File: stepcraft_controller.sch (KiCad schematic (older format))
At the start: 70 parts, among them J1 USB, J10 4th Axle, J11 Input2 Select, J2 Probe, J3 Spindle, J4 OutSelect, J6 Relay select, J7 Serial, J8 ISP, J9 X1, SW1 RST, U1 CP2102N-A01-GQFN24, U2 ADuM1201BR, U3 ADuM1201BR, U4 ATMEGA328P-AU, Y1 Crystal

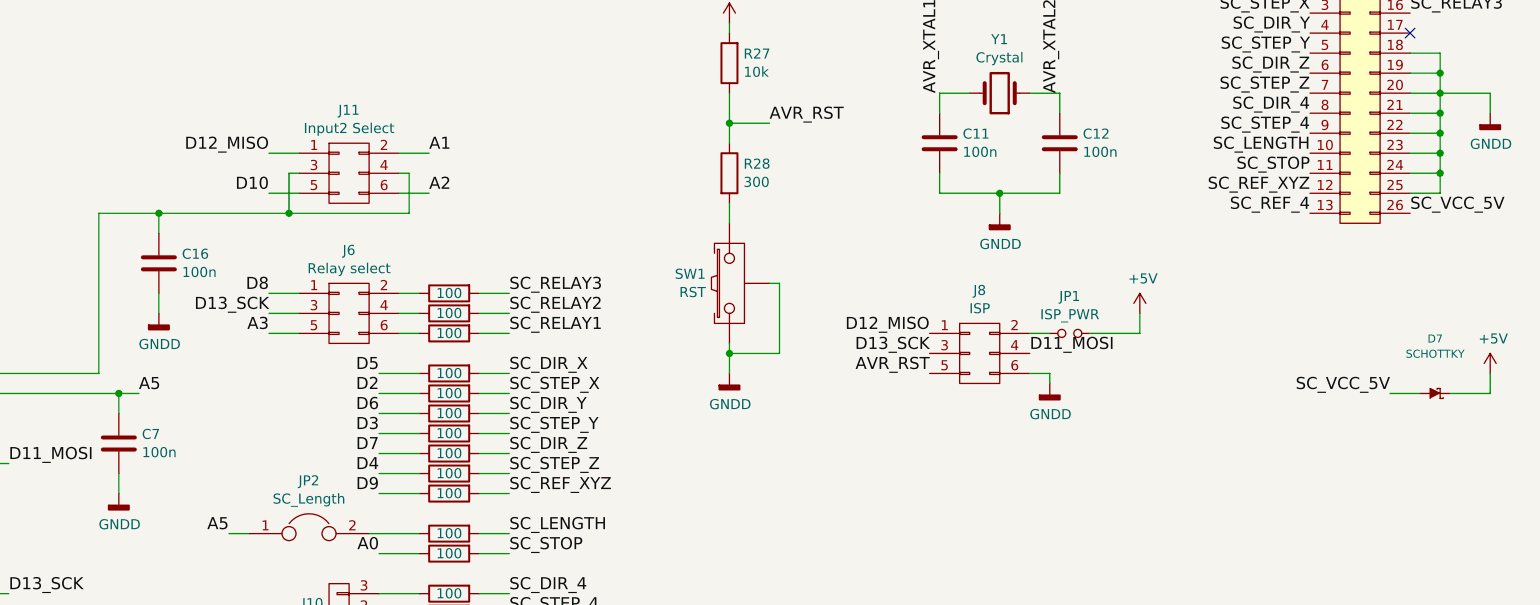
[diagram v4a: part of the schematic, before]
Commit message: Fix Diode symbol (was reversed), input dcouple caps value, X1 caps value, minor routing improvement.
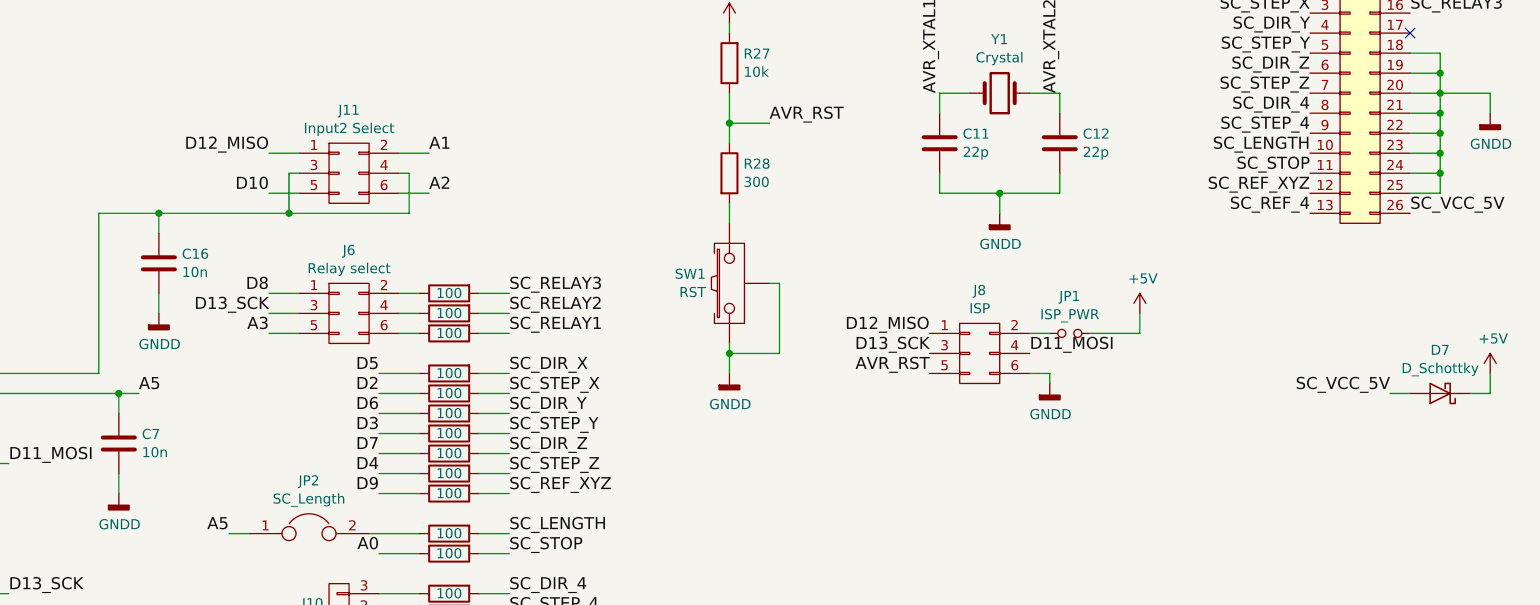
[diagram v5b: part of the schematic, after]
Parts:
- removed D7: SCHOTTKY, Diodes_SMD:D_SOD-123, symbol SCHOTTKY
- added D7: D_Schottky, Diodes_SMD:D_SOD-123, symbol D_Schottky
- C11, C12: value 100n -> 22p
- C16, C7: value 100n -> 10n
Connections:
- net +5V: now also D7.1 (K)
- net SC_VCC_5V: now also D7.2 (A)
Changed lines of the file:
@@
-	1    0    0    -1
-$EndComp
-$Comp
-L SCHOTTKY D7
-U 1 1 59977912
-P 10550 6250
-F 0 "D7" H 10575 6523 40  0000 C CNN
-F 1 "SCHOTTKY" H 10575 6447 40  0000 C CNN
-F 2 "Diodes_SMD:D_SOD-123" H 10575 6356 60  0001 C CNN
-F 3 "" H 10550 6250 60  0000 C CNN
-	1    10550 6250
 	1    0    0    -1
 $EndComp
@@
 P 8100 5000
 F 0 "C11" H 8215 5046 50  0000 L CNN
-F 1 "100n" H 8215 4955 50  0000 L CNN
+F 1 "22p" H 8215 4955 50  0000 L CNN
 F 2 "Capacitors_SMD:C_0805" H 8138 4850 50  0001 C CNN
 F 3 "" H 8100 5000 50  0001 C CNN
@@
 P 8700 5000
 F 0 "C12" H 8815 5046 50  0000 L CNN
-F 1 "100n" H 8815 4955 50  0000 L CNN
+F 1 "22p" H 8815 4955 50  0000 L CNN
 F 2 "Capacitors_SMD:C_0805" H 8738 4850 50  0001 C CNN
 F 3 "" H 8700 5000 50  0001 C CNN
@@
 P 4000 6500
 F 0 "C7" H 4115 6546 50  0000 L CNN
-F 1 "100n" H 4115 6455 50  0000 L CNN
+F 1 "10n" H 4115 6455 50  0000 L CNN
 F 2 "Capacitors_SMD:C_0805" H 4038 6350 50  0001 C CNN
 F 3 "" H 4000 6500 50  0001 C CNN
@@
 P 4200 5600
 F 0 "C16" H 4315 5646 50  0000 L CNN
-F 1 "100n" H 4315 5555 50  0000 L CNN
+F 1 "10n" H 4315 5555 50  0000 L CNN
 F 2 "Capacitors_SMD:C_0805" H 4238 5450 50  0001 C CNN
 F 3 "" H 4200 5600 50  0001 C CNN
@@
 Wire Wire Line
 	7050 4450 7050 4400
-Wire Wire Line
-	10350 6250 10500 6250
-Wire Wire Line
-	10650 6250 10850 6250
 Wire Wire Line
 	5850 2750 5850 2650
@@
 NoConn ~ 3650 2550
 NoConn ~ 3650 2450
+$Comp
+L D_Schottky D7
+U 1 1 59FC710B
+P 10600 6250
+F 0 "D7" H 10600 6034 50  0000 C CNN
+F 1 "D_Schottky" H 10600 6125 50  0000 C CNN
+F 2 "Diodes_SMD:D_SOD-123" H 10600 6250 50  0001 C CNN
+F 3 "" H 10600 6250 50  0001 C CNN
+	1    10600 6250
+	-1   0    0    1
+$EndComp
+Wire Wire Line
+	10350 6250 10450 6250
+Wire Wire Line
+	10750 6250 10850 6250
 $EndSCHEMATC

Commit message: Update to Kicad 5, add remarks about galvanic isolation
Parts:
- added R29: 10k (DNP), Resistors_SMD:R_0805, symbol Device:R
- C1, C10, C11, C12, C13, C14, C15, C16, C2, C3, C4, C5, C6, C7, C8, C9: symbol C -> Device:C
- D1, D2, D3, D4, D5, D6: value D_TVS -> TVS Diode; footprint Capacitors_SMD:C_0603 -> Diode_SMD:D_0603_1608Metric; symbol D_TVS -> Device:D_TVS
- D7: symbol D_Schottky -> Device:D_Schottky
- F1: symbol Polyfuse -> Device:Polyfuse
- J1: footprint iotta_footprints:conn_usb_B_micro_smd -> iotta_footprints:USB_Micro-B_2_Holes; symbol USB_OTG -> stepcraft_controller-rescue:USB_OTG
- J10, J4: symbol CONN_01X03 -> stepcraft_controller-rescue:CONN_01X03
- J11, J6, J8: symbol CONN_02X03 -> stepcraft_controller-rescue:CONN_02X03
- J2, J3: symbol Audio-Jack-3 -> stepcraft_controller-rescue:Audio-Jack-3
- J7: symbol CONN_01X02 -> stepcraft_controller-rescue:CONN_01X02
- J9: symbol Stepcraft_X1 -> iotta_wsn_rev2:Stepcraft_X1
- JP1: symbol Jumper_NO_Small -> Device:Jumper_NO_Small
- JP2: symbol Jumper -> Device:Jumper
- R1, R10, R11, R12, R13, R14, R15, R16, R17, R18, R19, R2, R20, R21, R22, R23, R24, R25, R26, R27, R28, R3, R4, R5, R6, R7, R8, R9: symbol R -> Device:R
- SW1: symbol SW_PUSH_SHIELD -> iotta_wsn_rev2:SW_PUSH_SHIELD
- U1: symbol CP2102N-A01-GQFN24 -> stepcraft_controller-rescue:CP2102N-A01-GQFN24
- U2, U3: symbol ADuM1201BR -> stepcraft_controller-rescue:ADuM1201BR
- U4: symbol ATMEGA328P-AU -> stepcraft_controller-rescue:ATMEGA328P-AU
- Y1: symbol Crystal -> Device:Crystal
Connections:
- net +5V: now also R29.2
- net AVR_RST: now also R29.1
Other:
- note added: "For use without galvanic separation:\n\n- Do not place U2 and U3 \n- Do not place C5, C6, C8, C9, R9, R10, R11\n- Place R5, R6, R7, R8"
- note added: "TVS Diodes, use for example Wurth 82356050050 \nProbably any 5V TVS/ESD suppressor will work\n\nFor added protection input resistors R1 and R2 may\nbe increased to a higher value. In that case one could\nprobably rely on the internat ESD protection in the ATMega."
- moved on the sheet: J7, R8
